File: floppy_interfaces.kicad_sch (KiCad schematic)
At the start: 22 parts, among them J13 Conn_01x04_Male, J14 Conn_02x17_Odd_Even, J16 Conn_01x04_Male, J6 SDF-60J for IEC 1541 serial p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, U1 74LS373, U2 74LVC374, U22 74LS06N, U3 74LVC374, U4 74LS373

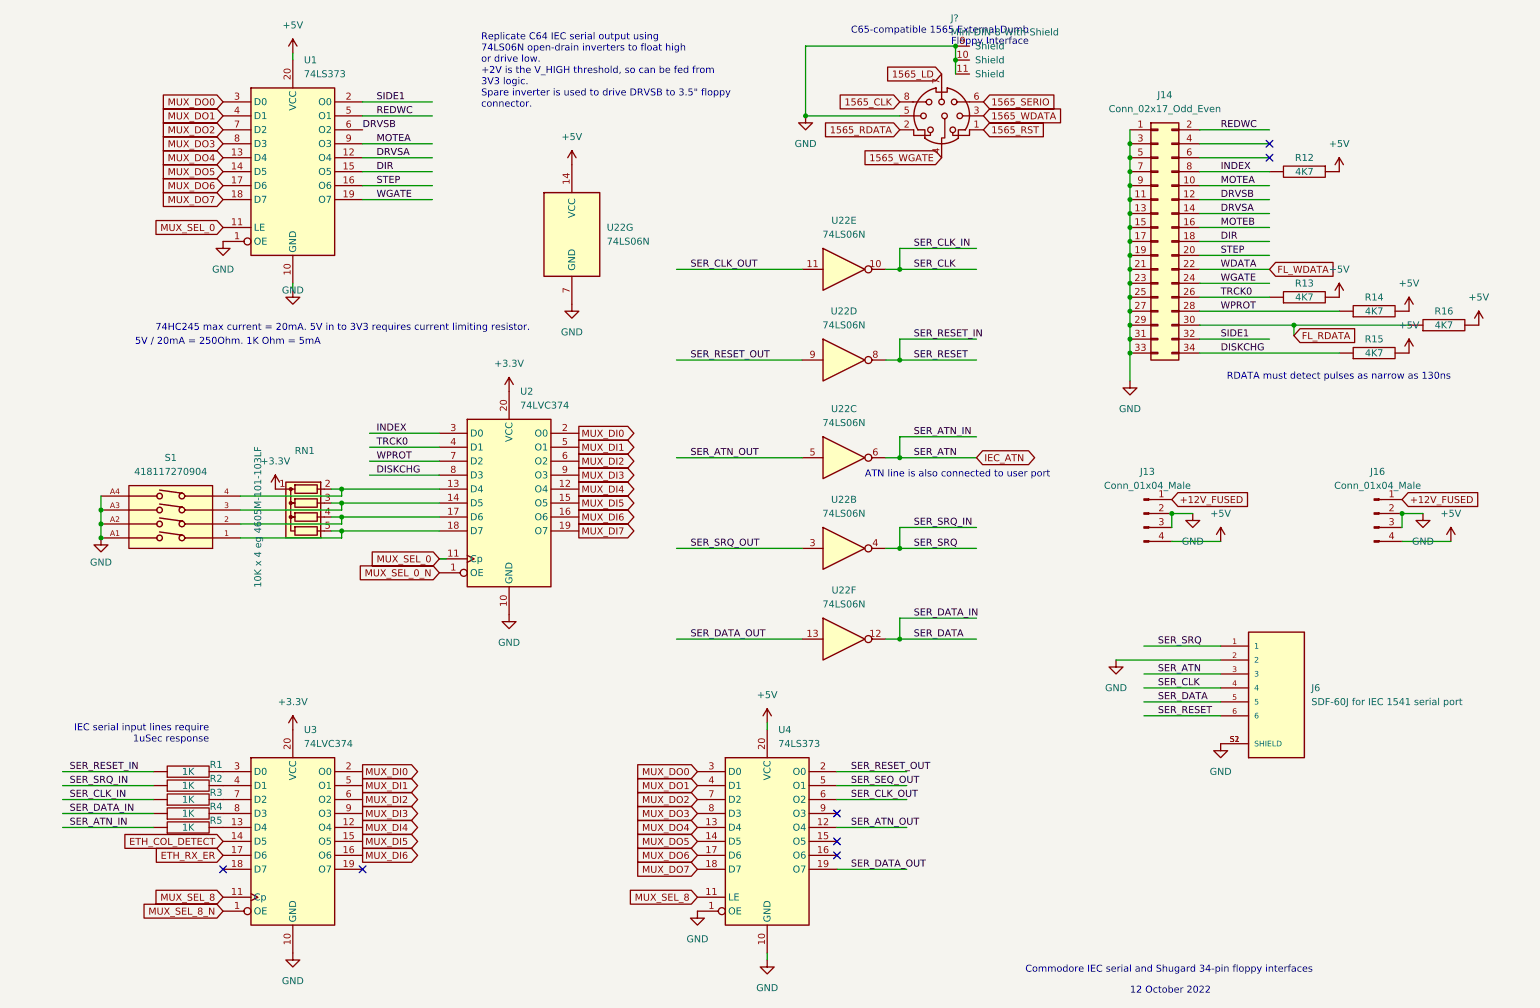
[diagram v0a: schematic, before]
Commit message: add 1565 interface #14
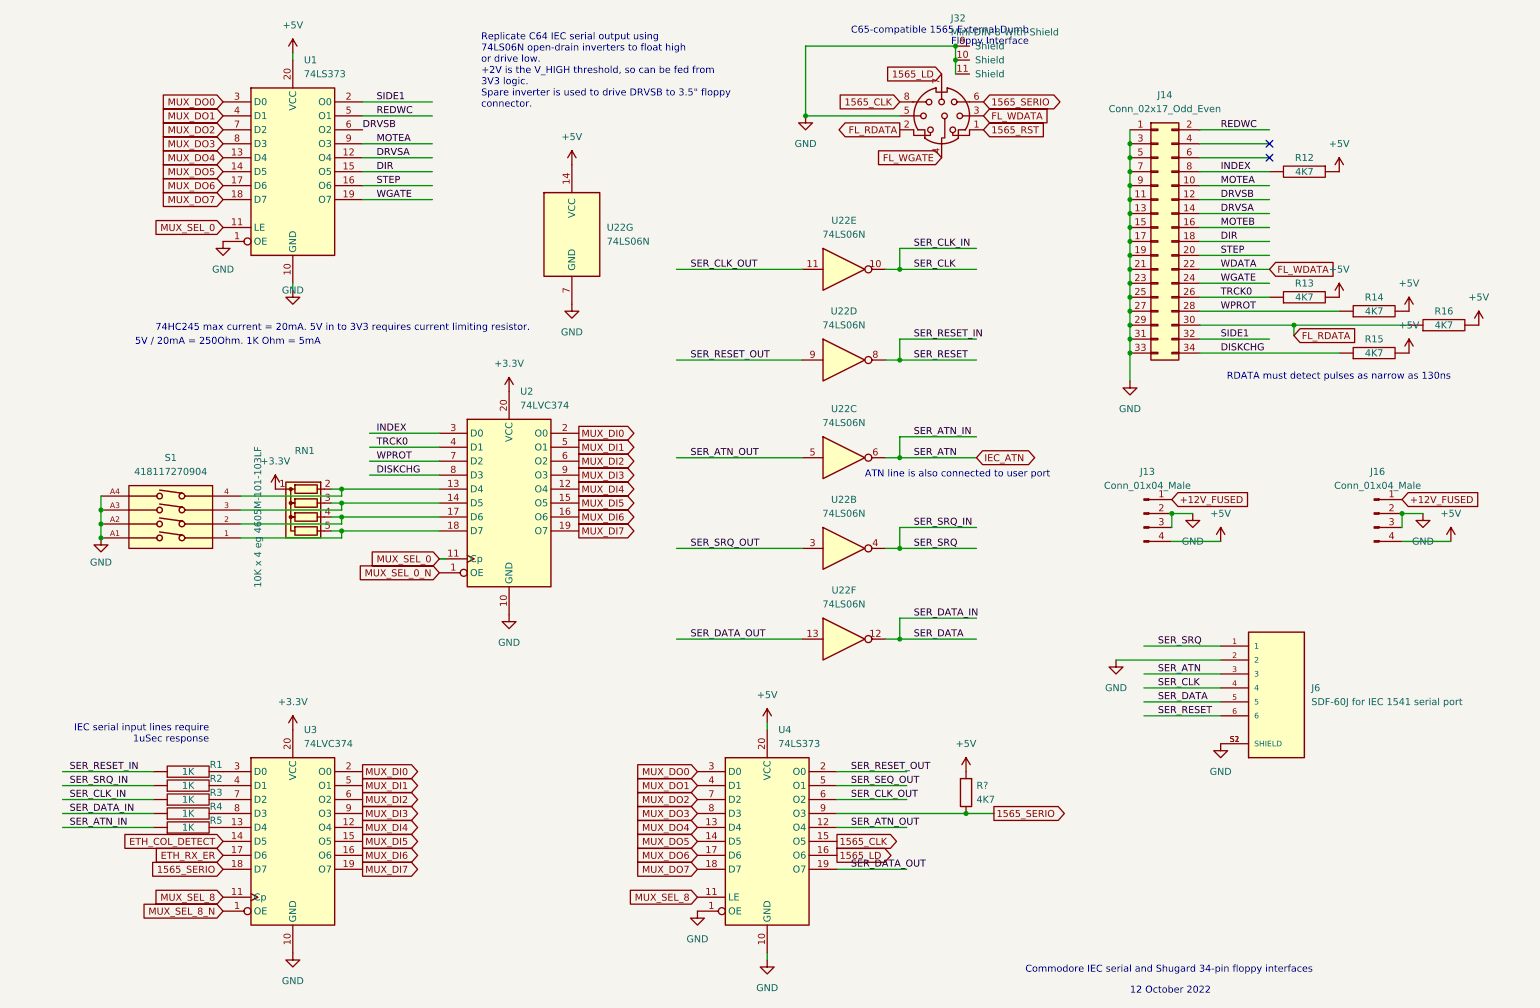
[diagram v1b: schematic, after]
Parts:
- added R?: 4K7, snapeda:Labeled Resistor, symbol Device:R
- gave numbers to parts that had none: 1
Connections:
- net 1565_RDATA is gone; now on net FL_RDATA: J32.2
- net 1565_WDATA is gone; now on net FL_WDATA: J32.3
- net +5V: now also R?.2
- net 1565_CLK: now also U4.15 (O5)
- net 1565_LD: now also U4.16 (O6)
- net 1565_SERIO: now also U3.18 (D7), U4.9 (O3), R?.1
- net MUX_DI7: now also U3.19 (O7)
- net 1565_WGATE renamed FL_WGATE
- no-connect marks 7 -> 2
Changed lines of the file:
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@@
   (junction (at 209.55 41.91) (diameter 0) (color 0 0 0 0)
   )
+  (junction (at 179.705 161.29) (diameter 0) (color 0 0 0 0)
+  )
   (junction (at 66.04 104.775) (diameter 0) (color 0 0 0 0)
   )
@@
   )
   (no_connect (at 234.95 39.37))
-  (no_connect (at 156.21 161.29))
-  (no_connect (at 44.45 171.45))
-  (no_connect (at 156.21 166.37))
   (no_connect (at 234.95 41.91))
-  (no_connect (at 69.85 171.45))
-  (no_connect (at 156.21 168.91))
   (wire (pts (xy 167.64 58.42) (xy 181.61 58.42))
     (stroke (width 0) (type default) (color 0 0 0 0))
@@
     (stroke (width 0) (type default) (color 0 0 0 0))
   )
+  (wire (pts (xy 179.705 161.29) (xy 184.785 161.29))
+    (stroke (width 0) (type default) (color 0 0 0 0))
+  )
   (wire (pts (xy 165.1 96.52) (xy 167.64 96.52))
     (stroke (width 0) (type default) (color 0 0 0 0))
@@
   )
   (wire (pts (xy 167.64 113.03) (xy 167.64 109.22))
+    (stroke (width 0) (type default) (color 0 0 0 0))
+  )
+  (wire (pts (xy 156.21 161.29) (xy 179.705 161.29))
     (stroke (width 0) (type default) (color 0 0 0 0))
   )
@@
     )
   )
+  (global_label "1565_CLK" (shape output) (at 156.21 166.37 0) (fields_autoplaced)
+    (effects (font (size 1.27 1.27)) (justify left))
+    (property "Intersheet References" "${INTERSHEET_REFS}" (id 0) (at 167.9969 166.2906 0)
+      (effects (font (size 1.27 1.27)) (justify left) hide)
+    )
+  )
   (global_label "MUX_DI0" (shape output) (at 109.22 92.075 0) (fields_autoplaced)
     (effects (font (size 1.27 1.27)) (justify left))
@@
     )
   )
-  (global_label "1565_SERIO" (shape input) (at 182.88 31.75 0) (fields_autoplaced)
+  (global_label "1565_SERIO" (shape bidirectional) (at 182.88 31.75 0) (fields_autoplaced)
     (effects (font (size 1.27 1.27)) (justify left))
     (property "Intersheet References" "${INTERSHEET_REFS}" (id 0) (at 196.6626 31.6706 0)
@@
     )
   )
+  (global_label "1565_LD" (shape output) (at 156.21 168.91 0) (fields_autoplaced)
+    (effects (font (size 1.27 1.27)) (justify left))
+    (property "Intersheet References" "${INTERSHEET_REFS}" (id 0) (at 166.7269 168.8306 0)
+      (effects (font (size 1.27 1.27)) (justify left) hide)
+    )
+  )
   (global_label "1565_RST" (shape input) (at 182.88 36.83 0) (fields_autoplaced)
     (effects (font (size 1.27 1.27)) (justify left))
@@
     )
   )
-  (global_label "1565_WDATA" (shape input) (at 182.88 34.29 0) (fields_autoplaced)
+  (global_label "FL_WDATA" (shape input) (at 182.88 34.29 0) (fields_autoplaced)
     (effects (font (size 1.27 1.27)) (justify left))
-    (property "Intersheet References" "${INTERSHEET_REFS}" (id 0) (at 196.965 34.2106 0)
+    (property "Intersheet References" "${INTERSHEET_REFS}" (id 0) (at 194.2436 34.2106 0)
       (effects (font (size 1.27 1.27)) (justify left) hide)
     )
@@
     )
   )
-  (global_label "1565_WGATE" (shape input) (at 175.26 41.91 180) (fields_autoplaced)
-    (effects (font (size 1.27 1.27)) (justify right))
-    (property "Intersheet References" "${INTERSHEET_REFS}" (id 0) (at 161.1145 41.8306 0)
+  (global_label "FL_WGATE" (shape input) (at 175.26 41.91 180) (fields_autoplaced)
+    (effects (font (size 1.27 1.27)) (justify right))
+    (property "Intersheet References" "${INTERSHEET_REFS}" (id 0) (at 163.8359 41.8306 0)
       (effects (font (size 1.27 1.27)) (justify right) hide)
     )
@@
     )
   )
+  (global_label "1565_SERIO" (shape input) (at 44.45 171.45 180) (fields_autoplaced)
+    (effects (font (size 1.27 1.27)) (justify right))
+    (property "Intersheet References" "${INTERSHEET_REFS}" (id 0) (at 30.6674 171.3706 0)
+      (effects (font (size 1.27 1.27)) (justify right) hide)
+    )
+  )
   (global_label "MUX_DO4" (shape input) (at 44.45 41.91 180) (fields_autoplaced)
     (effects (font (size 1.27 1.27)) (justify right))
@@
     )
   )
+  (global_label "1565_SERIO" (shape output) (at 184.785 161.29 0) (fields_autoplaced)
+    (effects (font (size 1.27 1.27)) (justify left))
+    (property "Intersheet References" "${INTERSHEET_REFS}" (id 0) (at 198.5676 161.2106 0)
+      (effects (font (size 1.27 1.27)) (justify left) hide)
+    )
+  )
   (global_label "1565_CLK" (shape input) (at 167.64 31.75 180) (fields_autoplaced)
     (effects (font (size 1.27 1.27)) (justify right))
@@
     )
   )
+  (global_label "MUX_DI7" (shape output) (at 69.85 171.45 0) (fields_autoplaced)
+    (effects (font (size 1.27 1.27)) (justify left))
+    (property "Intersheet References" "${INTERSHEET_REFS}" (id 0) (at 80.3064 171.3706 0)
+      (effects (font (size 1.27 1.27)) (justify left) hide)
+    )
+  )
   (global_label "MUX_DI3" (shape output) (at 69.85 161.29 0) (fields_autoplaced)
     (effects (font (size 1.27 1.27)) (justify left))
@@
     )
   )
-  (global_label "1565_RDATA" (shape input) (at 167.64 36.83 180) (fields_autoplaced)
-    (effects (font (size 1.27 1.27)) (justify right))
-    (property "Intersheet References" "${INTERSHEET_REFS}" (id 0) (at 153.7364 36.7506 0)
+  (global_label "FL_RDATA" (shape output) (at 167.64 36.83 180) (fields_autoplaced)
+    (effects (font (size 1.27 1.27)) (justify right))
+    (property "Intersheet References" "${INTERSHEET_REFS}" (id 0) (at 156.4579 36.7506 0)
       (effects (font (size 1.27 1.27)) (justify right) hide)
     )
@@
   (symbol (lib_id "power:GND") (at 150.495 34.29 0) (unit 1)
     (in_bom yes) (on_board yes) (fields_autoplaced)
-    (property "Reference" "#PWR?" (id 0) (at 150.495 40.64 0)
+    (property "Reference" "#PWR0335" (id 0) (at 150.495 40.64 0)
       (effects (font (size 1.27 1.27)) hide)
     )
@@
     (pin "1")
   )
+  (symbol (lib_id "power:+5V") (at 179.705 153.67 0) (unit 1)
+    (in_bom yes) (on_board yes) (fields_autoplaced)
+    (property "Reference" "#PWR?" (id 0) (at 179.705 157.48 0)
+      (effects (font (size 1.27 1.27)) hide)
+    )
+    (property "Value" "+5V" (id 1) (at 179.705 148.59 0))
+    (property "Footprint" "" (id 2) (at 179.705 153.67 0)
+      (effects (font (size 1.27 1.27)) hide)
+    )
+    (property "Datasheet" "" (id 3) (at 179.705 153.67 0)
+      (effects (font (size 1.27 1.27)) hide)
+    )
+    (pin "1")
+  )
   (symbol (lib_id "power:GND") (at 262.89 106.68 0) (unit 1)
     (in_bom yes) (on_board yes) (fields_autoplaced)
@@
     (pin "1")
   )
+  (symbol (lib_id "Device:R") (at 179.705 157.48 180) (unit 1)
+    (in_bom yes) (on_board yes) (fields_autoplaced)
+    (property "Reference" "R?" (id 0) (at 181.61 156.2099 0)
+      (effects (font (size 1.27 1.27)) (justify right))
+    )
+    (property "Value" "4K7" (id 1) (at 181.61 158.7499 0)
+      (effects (font (size 1.27 1.27)) (justify right))
+    )
+    (property "Footprint" "snapeda:Labeled Resistor" (id 2) (at 181.483 157.48 90)
+      (effects (font (size 1.27 1.27)) hide)
+    )
+    (property "Datasheet" "~" (id 3) (at 179.705 157.48 0)
+      (effects (font (size 1.27 1.27)) hide)
+    )
+    (pin "1")
+    (pin "2")
+  )
   (symbol (lib_id "74xx:74LS06N") (at 157.48 96.52 0) (unit 3)
     (in_bom yes) (on_board yes) (fields_autoplaced)
@@
   (symbol (lib_id "00Project-SDF-60J:Mini-DIN-8-With-Shield") (at 175.26 34.29 0) (unit 1)
     (in_bom yes) (on_board yes) (fields_autoplaced)
-    (property "Reference" "J?" (id 0) (at 176.9111 16.51 0)
+    (property "Reference" "J32" (id 0) (at 176.9111 16.51 0)
       (effects (font (size 1.27 1.27)) (justify left))
     )

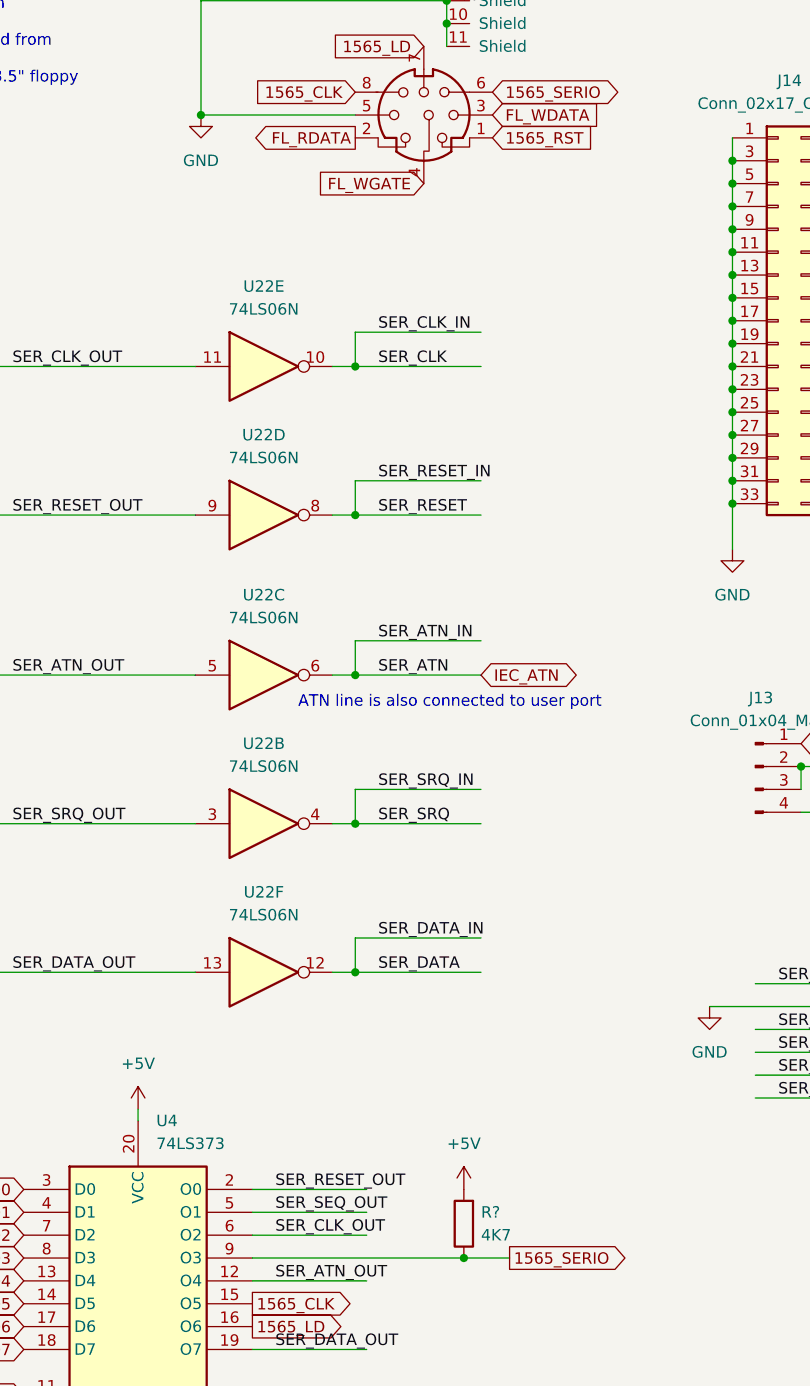
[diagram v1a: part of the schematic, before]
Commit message: route 1565 and tape connectors #14
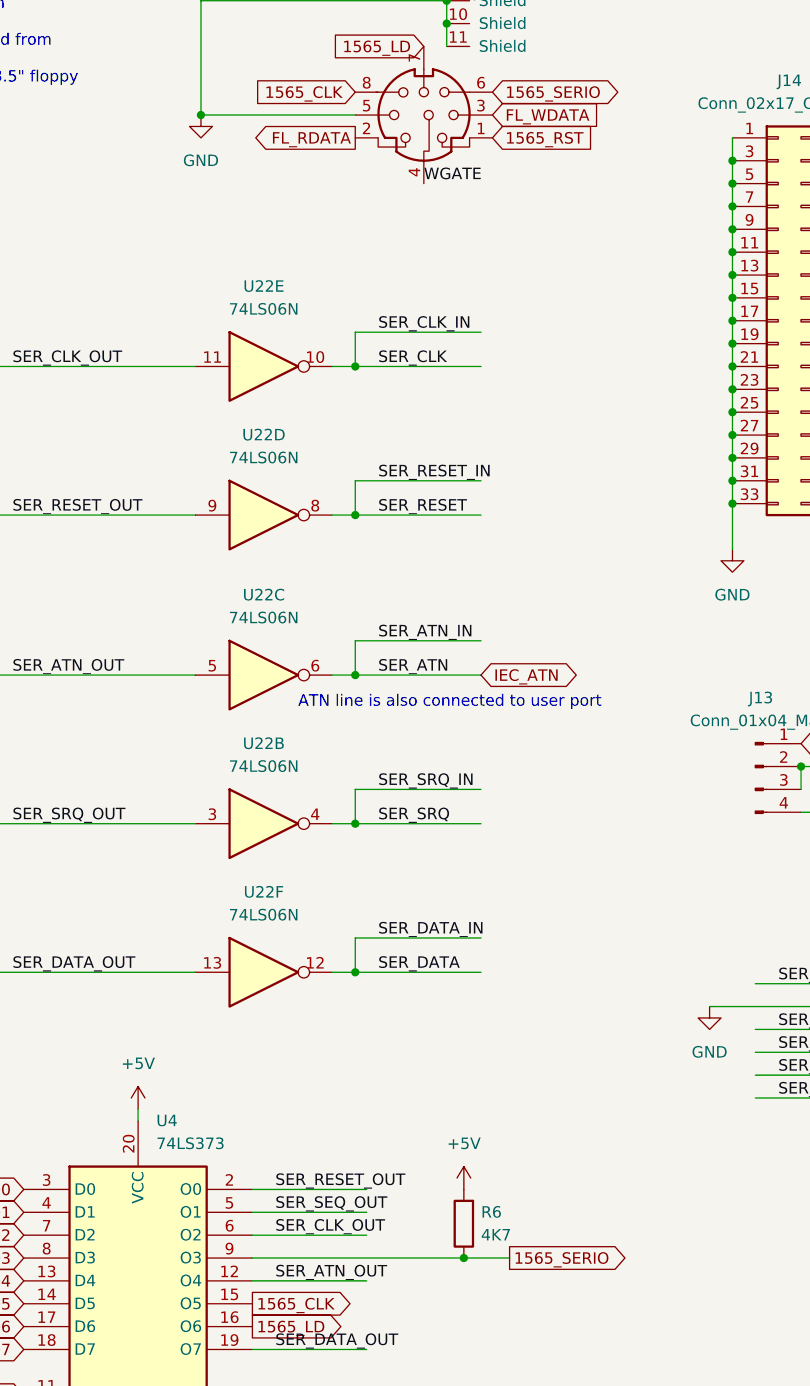
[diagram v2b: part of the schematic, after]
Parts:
- gave numbers to parts that had none: 1
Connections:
- net FL_WGATE is gone; now on net WGATE: J32.4
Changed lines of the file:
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@@
+    (effects (font (size 1.27 1.27)) (justify left bottom))
+  )
+  (label "WGATE" (at 175.26 41.91 0)
     (effects (font (size 1.27 1.27)) (justify left bottom))
   )
@@
     (effects (font (size 1.27 1.27)) (justify right))
     (property "Intersheet References" "${INTERSHEET_REFS}" (id 0) (at 33.2679 39.2906 0)
-      (effects (font (size 1.27 1.27)) (justify right) hide)
-    )
-  )
-  (global_label "FL_WGATE" (shape input) (at 175.26 41.91 180) (fields_autoplaced)
-    (effects (font (size 1.27 1.27)) (justify right))
-    (property "Intersheet References" "${INTERSHEET_REFS}" (id 0) (at 163.8359 41.8306 0)
       (effects (font (size 1.27 1.27)) (justify right) hide)
     )
@@
   (symbol (lib_id "power:+5V") (at 179.705 153.67 0) (unit 1)
     (in_bom yes) (on_board yes) (fields_autoplaced)
-    (property "Reference" "#PWR?" (id 0) (at 179.705 157.48 0)
+    (property "Reference" "#PWR0336" (id 0) (at 179.705 157.48 0)
       (effects (font (size 1.27 1.27)) hide)
     )
@@
   (symbol (lib_id "Device:R") (at 179.705 157.48 180) (unit 1)
     (in_bom yes) (on_board yes) (fields_autoplaced)
-    (property "Reference" "R?" (id 0) (at 181.61 156.2099 0)
+    (property "Reference" "R6" (id 0) (at 181.61 156.2099 0)
       (effects (font (size 1.27 1.27)) (justify right))
     )

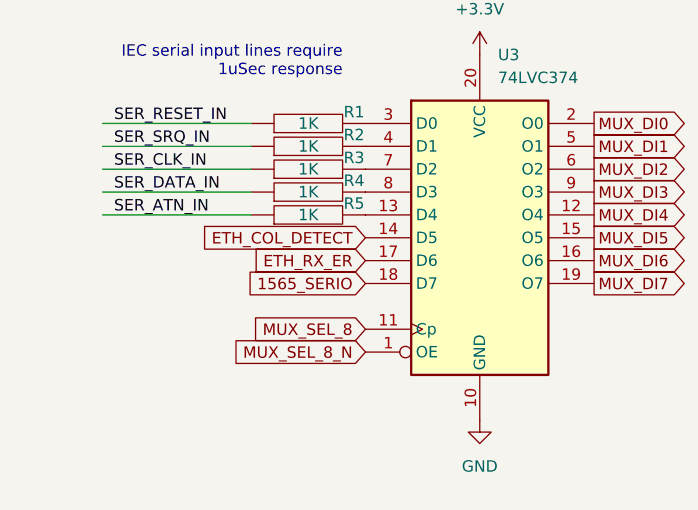
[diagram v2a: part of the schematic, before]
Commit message: work on routing user port
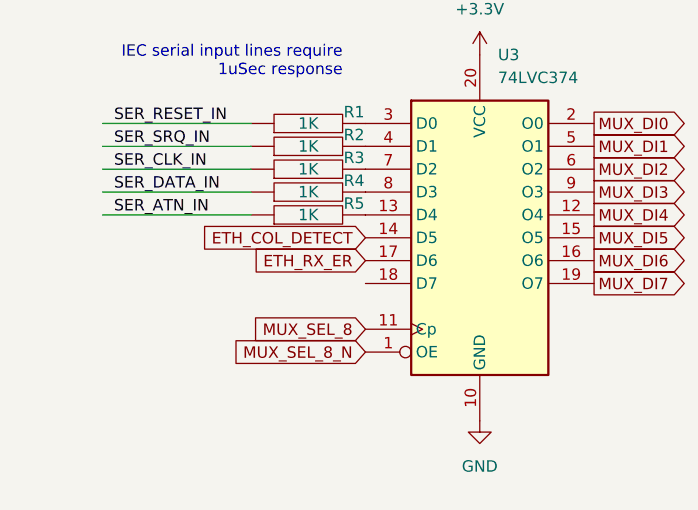
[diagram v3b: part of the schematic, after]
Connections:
- net 1565_SERIO: no longer U3.18 (D7)
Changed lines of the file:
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@@
-    )
-  )
-  (global_label "1565_SERIO" (shape input) (at 44.45 171.45 180) (fields_autoplaced)
-    (effects (font (size 1.27 1.27)) (justify right))
-    (property "Intersheet References" "${INTERSHEET_REFS}" (id 0) (at 30.6674 171.3706 0)
-      (effects (font (size 1.27 1.27)) (justify right) hide)
     )
   )
